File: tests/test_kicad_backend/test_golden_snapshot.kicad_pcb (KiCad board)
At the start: 2 copper layers, 24.8 x 22.7 mm, 1 part

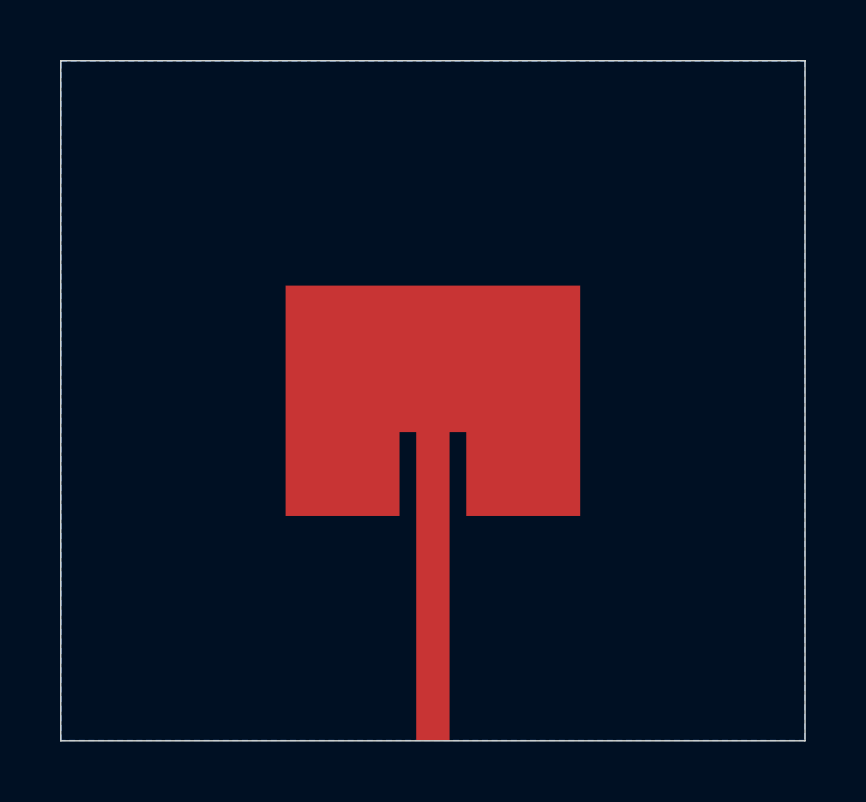
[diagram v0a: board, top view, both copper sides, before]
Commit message: Close the loop: MSL port, cos^4 inset model, simulation-feedback tuning
Validation ladder against openEMS (Docker): upstream Simple_Patch_Antenna
tutorial reproduced through the runner (2.29 GHz, -29 dB); probe-fed bare
patch confirmed synthesis dimensions (9.70 GHz, -11 dB, ~30 ohm at inset).
The full design's poor match traced to two causes, both fixed: mesh lines
deduped by tolerance (near-coincident lines collapsed the FDTD timestep) and
the cos^2 inset-resistance model, replaced by the standard cos^4 notched-feed
profile. Added a microstrip (MSL) port model as the default edge-launch
excitation and a tune loop that corrects length/inset from measured resonance
and input resistance. MVP acceptance passes: spec -> synthesis -> DRC-clean
KiCad board -> openEMS -> report; f_res 9.84 GHz, S11 -11.5 dB, D 6.8 dBi.

Co-Authored-By: Claude Fable 5 <noreply@anthropic.com>
Claude-Session: https://claude.ai/code/session_01En24RksRv1HE8U3wnsYN4i
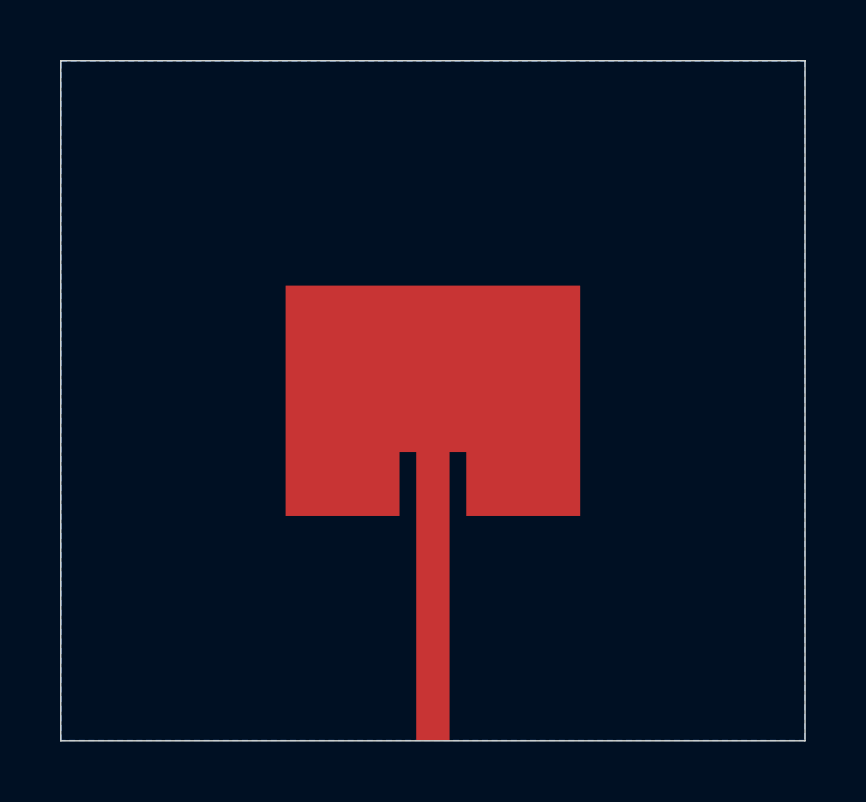
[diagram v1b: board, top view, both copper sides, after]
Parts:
- moved ? 0.33 mm to (9.39, 14.1)
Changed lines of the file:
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@@
 		"antenna_cad:radiator_0"
 		(layer "F.Cu")
-		(at 9.393813 13.776174)
+		(at 9.393813 14.108747)
 		(attr smd board_only exclude_from_pos_files exclude_from_bom allow_missing_courtyard)
 		(pad
@@
 			(primitives
 				(gr_poly
-					(pts (xy 2.455007 -1.397926) (xy 1.899002 -1.397926) (xy 1.899002 1.397926) (xy -1.899002 1.397926) (xy -1.899002 -6.281362) (xy 7.921026 -6.281362) (xy 7.921026 1.397926) (xy 4.123022 1.397926) (xy 4.123022 -1.397926) (xy 3.567017 -1.397926) (xy 3.567017 8.882738) (xy 2.455007 8.882738))
+					(pts (xy 2.455007 -1.065353) (xy 1.899002 -1.065353) (xy 1.899002 1.065353) (xy -1.899002 1.065353) (xy -1.899002 -6.613936) (xy 7.921026 -6.613936) (xy 7.921026 1.065353) (xy 4.123022 1.065353) (xy 4.123022 -1.065353) (xy 3.567017 -1.065353) (xy 3.567017 8.550164) (xy 2.455007 8.550164))
 					(width 0)
 					(fill yes)
